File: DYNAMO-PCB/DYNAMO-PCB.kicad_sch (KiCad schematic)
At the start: 12 parts, among them J13 Conn_01x02_Pin, J18 USB3_A, J21 USB3_A, J22 USB3_A, J23 USB3_A, J24 USB3_A, J25 USB3_A, J29 USB_C_Receptacle_USB2.0_16P, J3 Conn_01x03_Pin

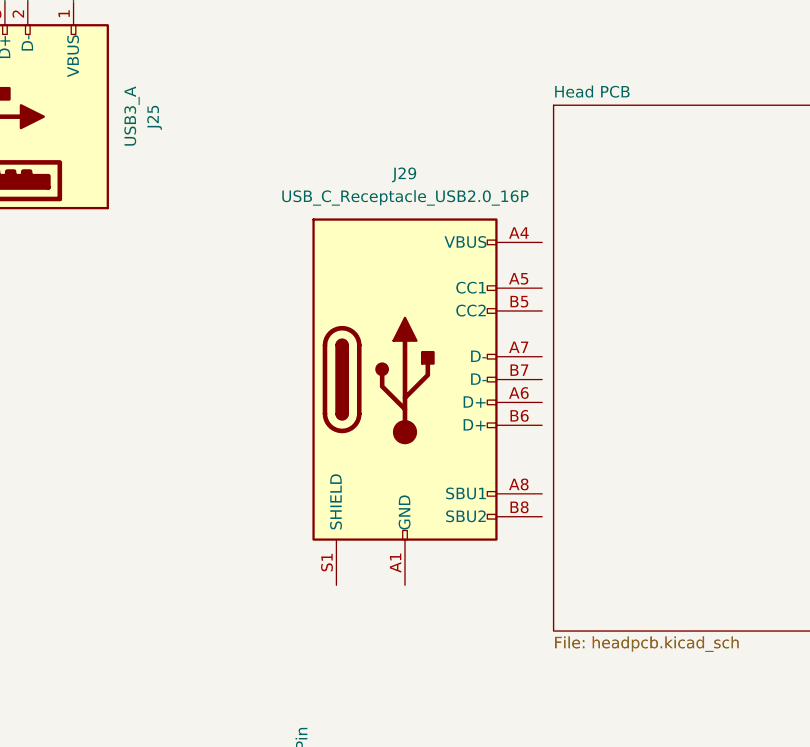
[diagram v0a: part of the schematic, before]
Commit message: wired headpcb sch
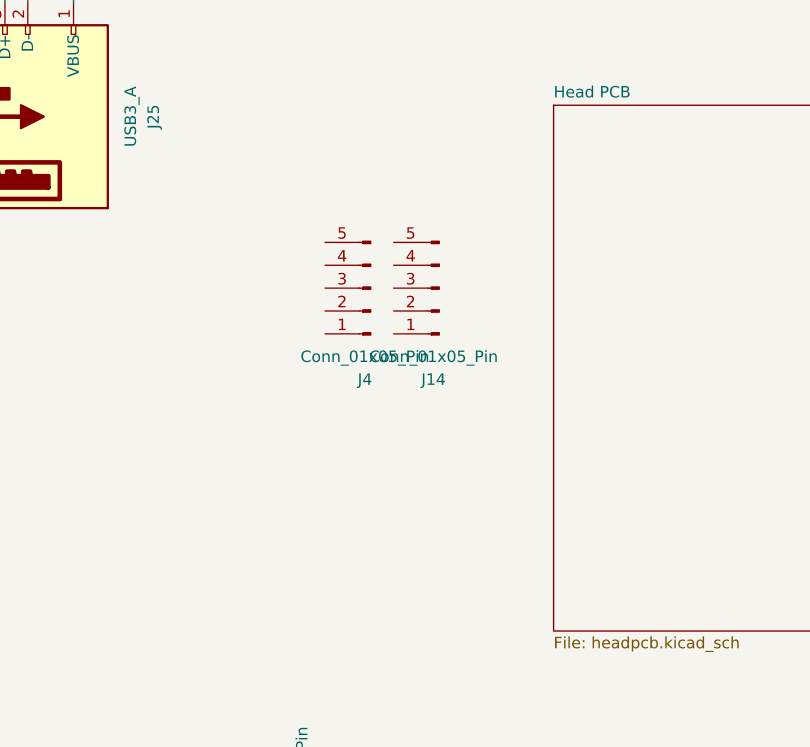
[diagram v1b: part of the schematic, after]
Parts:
- removed J29: USB_C_Receptacle_USB2.0_16P, Connector_USB:USB_C_Receptacle_GCT_USB4105-xx-A_16P_TopMnt_Horizontal, symbol Connector:USB_C_Receptacle_USB2.0_16P
- added J14, J4: Conn_01x05_Pin, Connector_PinHeader_2.54mm:PinHeader_1x05_P2.54mm_Vertical, symbol Connector:Conn_01x05_Pin
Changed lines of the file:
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@@
+	)
+	(symbol
+		(lib_id "Connector:Conn_01x05_Pin")
+		(at 218.44 81.28 180)
+		(unit 1)
+		(exclude_from_sim no)
+		(in_bom yes)
+		(on_board yes)
+		(dnp no)
+		(fields_autoplaced yes)
+		(property "Reference" "J4"
+			(at 217.805 91.44 0)
+			(effects
+				(font
+					(size 1.27 1.27)
+				)
+			)
+		)
+		(property "Value" "Conn_01x05_Pin"
+			(at 217.805 88.9 0)
+			(effects
+				(font
+					(size 1.27 1.27)
+				)
+			)
+		)
+		(property "Footprint" "Connector_PinHeader_2.54mm:PinHeader_1x05_P2.54mm_Vertical"
+			(at 218.44 81.28 0)
+			(effects
+				(font
+					(size 1.27 1.27)
+				)
+				(hide yes)
+			)
+		)
+		(property "Datasheet" "~"
+			(at 218.44 81.28 0)
+			(effects
+				(font
+					(size 1.27 1.27)
+				)
+				(hide yes)
+			)
+		)
+		(property "Description" "Generic connector, single row, 01x05, script generated"
+			(at 218.44 81.28 0)
+			(effects
+				(font
+					(size 1.27 1.27)
+				)
+				(hide yes)
+			)
+		)
+		(pin "1"
+		)
+		(pin "2"
+		)
+		(pin "5"
+		)
+		(pin "3"
+		)
+		(pin "4"
+		)
+		(instances
+			(project ""
+				(path "/2ca9dd43-411d-4cc5-8a4b-ed00d72bae91"
+					(reference "J4")
+					(unit 1)
+				)
+			)
+		)
 	)
 	(symbol
@@
 	)
 	(symbol
-		(lib_id "Connector:USB_C_Receptacle_USB2.0_16P")
-		(at 222.25 91.44 0)
-		(unit 1)
-		(exclude_from_sim no)
-		(in_bom yes)
-		(on_board yes)
-		(dnp no)
-		(fields_autoplaced yes)
-		(property "Reference" "J29"
-			(at 222.25 68.58 0)
-			(effects
-				(font
-					(size 1.27 1.27)
-				)
-			)
-		)
-		(property "Value" "USB_C_Receptacle_USB2.0_16P"
-			(at 222.25 71.12 0)
-			(effects
-				(font
-					(size 1.27 1.27)
-				)
-			)
-		)
-		(property "Footprint" "Connector_USB:USB_C_Receptacle_GCT_USB4105-xx-A_16P_TopMnt_Horizontal"
-			(at 226.06 91.44 0)
-			(effects
-				(font
-					(size 1.27 1.27)
-				)
-				(hide yes)
-			)
-		)
-		(property "Datasheet" "https://www.usb.org/sites/default/files/documents/usb_type-c.zip"
-			(at 226.06 91.44 0)
-			(effects
-				(font
-					(size 1.27 1.27)
-				)
-				(hide yes)
-			)
-		)
-		(property "Description" "USB 2.0-only 16P Type-C Receptacle connector"
-			(at 222.25 91.44 0)
-			(effects
-				(font
-					(size 1.27 1.27)
-				)
-				(hide yes)
-			)
-		)
-		(pin "A1"
-		)
-		(pin "B12"
-		)
-		(pin "B9"
-		)
-		(pin "A4"
-		)
-		(pin "S1"
-		)
-		(pin "A12"
-		)
-		(pin "B1"
-		)
-		(pin "A9"
-		)
-		(pin "B4"
-		)
-		(pin "A7"
-		)
-		(pin "A5"
-		)
-		(pin "B6"
-		)
-		(pin "B5"
-		)
-		(pin "B8"
-		)
-		(pin "B7"
-		)
-		(pin "A6"
-		)
-		(pin "A8"
-		)
-		(instances
-			(project "DYNAMO-PCB"
-				(path "/2ca9dd43-411d-4cc5-8a4b-ed00d72bae91"
-					(reference "J29")
-					(unit 1)
-				)
-			)
-		)
-	)
-	(symbol
 		(lib_id "Connector:USB3_A")
 		(at 101.6 62.23 270)
@@
 					(unit 1)
 				)
+			)
+		)
+	)
+	(symbol
+		(lib_id "Connector:Conn_01x05_Pin")
+		(at 226.06 81.28 180)
+		(unit 1)
+		(exclude_from_sim no)
+		(in_bom yes)
+		(on_board yes)
+		(dnp no)
+		(fields_autoplaced yes)
+		(property "Reference" "J14"
+			(at 225.425 91.44 0)
+			(effects
+				(font
+					(size 1.27 1.27)
+				)
+			)
+		)
+		(property "Value" "Conn_01x05_Pin"
+			(at 225.425 88.9 0)
+			(effects
+				(font
+					(size 1.27 1.27)
+				)
+			)
+		)
+		(property "Footprint" "Connector_PinHeader_2.54mm:PinHeader_1x05_P2.54mm_Vertical"
+			(at 226.06 81.28 0)
+			(effects
+				(font
+					(size 1.27 1.27)
+				)
+				(hide yes)
+			)
+		)
+		(property "Datasheet" "~"
+			(at 226.06 81.28 0)
+			(effects
+				(font
+					(size 1.27 1.27)
+				)
+				(hide yes)
+			)
+		)
+		(property "Description" "Generic connector, single row, 01x05, script generated"
+			(at 226.06 81.28 0)
+			(effects
+				(font
+					(size 1.27 1.27)
+				)
+				(hide yes)
+			)
+		)
+		(pin "1"
+		)
+		(pin "2"
+		)
+		(pin "5"
+		)
+		(pin "3"
+		)
+		(pin "4"
+		)
+		(instances
+			(project "DYNAMO-PCB"
+				(path "/2ca9dd43-411d-4cc5-8a4b-ed00d72bae91"
+					(reference "J14")
+					(unit 1)
+				)

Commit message: schematic wip
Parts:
- removed J14, J4: Conn_01x05_Pin, Connector_PinHeader_2.54mm:PinHeader_1x05_P2.54mm_Vertical, symbol Connector:Conn_01x05_Pin
- added J34: Conn_02x05_Counter_Clockwise, Connector_PinHeader_2.54mm:PinHeader_2x05_P2.54mm_Vertical, symbol Connector_Generic:Conn_02x05_Counter_Clockwise
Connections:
- net GND: now reaches J22.4 (GND), J24.4 (GND)
- net GND: now also C1.2, J13.2 (Pin_2), J18.4 (GND), J21.4 (GND), J23.4 (GND), J25.4 (GND), J3.3 (Pin_3), J34.9 (Pin_9)
- net at J3.1 (Pin_1): now also R1.2
- net Power Distribution/+5V peripherals: now reaches J3.2 (Pin_2)
- net Power Distribution/+5V peripherals: now also C1.1, J13.1 (Pin_1), J34.10 (Pin_10)
- net at A1.11 (D6): now also R1.1
- net at A1.12 (D13): now also J34.8 (Pin_8)
- net at A1.16 (D11): now also J34.7 (Pin_7)
- net at A1.17 (D3/SCL): now also J34.4 (Pin_4)
- net at A1.18 (D10): now also J34.6 (Pin_6)
- net at A1.19 (D2/SDA): now also J34.5 (Pin_5)
- net at A1.20 (D9): now also J34.3 (Pin_3)
- net at A1.22 (D8): now also J34.1 (Pin_1)
- net at A1.24 (D7): now also J34.2 (Pin_2)
- no-connect marks 0 -> 79
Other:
- sheet Power Distribution ports: added +5V peripherals, GND peripherals; removed none
- moved on the sheet: A1A, A1B, C1, J13, J3, R1

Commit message: schematic wip
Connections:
- net Power Distribution/+5V peripherals: now also J3.1 (Pin_1); no longer J3.2 (Pin_2)
- net at R1.2: now also J3.2 (Pin_2); no longer J3.1 (Pin_1)
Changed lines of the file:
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@@
 	(paper "A4")
 	(junction
-		(at 132.08 156.21)
+		(at 128.27 157.48)
 		(diameter 0)
 		(color 0 0 0 0)
@@
 	)
 	(junction
-		(at 132.08 162.56)
-		(diameter 0)
-		(color 0 0 0 0)
-	)
-	(junction
 		(at 173.99 162.56)
 		(diameter 0)
@@
 	)
 	(junction
+		(at 128.27 160.02)
+		(diameter 0)
+		(color 0 0 0 0)
+	)
+	(junction
 		(at 151.13 167.64)
 		(diameter 0)
@@
 	(wire
 		(pts
-			(xy 128.27 160.02) (xy 133.35 160.02)
-		)
-		(stroke
-			(width 0)
-			(type default)
-		)
-	)
-	(wire
-		(pts
 			(xy 229.87 91.44) (xy 228.6 90.17)
 		)
@@
 	(wire
 		(pts
+			(xy 147.32 162.56) (xy 137.16 162.56)
+		)
+		(stroke
+			(width 0)
+			(type default)
+		)
+	)
+	(wire
+		(pts
 			(xy 83.82 67.31) (xy 80.01 63.5)
 		)
@@
 	(wire
 		(pts
-			(xy 132.08 156.21) (xy 133.35 154.94)
+			(xy 130.81 157.48) (xy 133.35 154.94)
 		)
 		(stroke
@@
 	(wire
 		(pts
-			(xy 133.35 160.02) (xy 137.16 156.21)
-		)
-		(stroke
-			(width 0)
-			(type default)
-		)
-	)
-	(wire
-		(pts
 			(xy 157.48 67.31) (xy 154.94 64.77)
 		)
@@
 	(wire
 		(pts
-			(xy 132.08 162.56) (xy 147.32 162.56)
-		)
-		(stroke
-			(width 0)
-			(type default)
-		)
-	)
-	(wire
-		(pts
 			(xy 129.54 44.45) (xy 129.54 49.53)
 		)
@@
 	(wire
 		(pts
+			(xy 137.16 162.56) (xy 134.62 160.02)
+		)
+		(stroke
+			(width 0)
+			(type default)
+		)
+	)
+	(wire
+		(pts
 			(xy 132.08 110.49) (xy 130.81 109.22)
 		)
@@
 	(wire
 		(pts
-			(xy 129.54 166.37) (xy 119.38 166.37)
+			(xy 137.16 132.08) (xy 137.16 160.02)
+		)
+		(stroke
+			(width 0)
+			(type default)
+		)
+	)
+	(wire
+		(pts
+			(xy 129.54 166.37) (xy 121.92 166.37)
 		)
 		(stroke
@@
 	(wire
 		(pts
-			(xy 132.08 156.21) (xy 132.08 162.56)
-		)
-		(stroke
-			(width 0)
-			(type default)
-		)
-	)
-	(wire
-		(pts
 			(xy 213.36 92.71) (xy 215.9 92.71)
 		)
@@
 	(wire
 		(pts
+			(xy 128.27 162.56) (xy 134.62 162.56)
+		)
+		(stroke
+			(width 0)
+			(type default)
+		)
+	)
+	(wire
+		(pts
 			(xy 200.66 80.01) (xy 213.36 92.71)
 		)
@@
 	(wire
 		(pts
-			(xy 130.81 157.48) (xy 132.08 156.21)
-		)
-		(stroke
-			(width 0)
-			(type default)
-		)
-	)
-	(wire
-		(pts
 			(xy 80.01 63.5) (xy 80.01 30.48)
 		)
@@
 	(wire
 		(pts
+			(xy 128.27 157.48) (xy 120.65 157.48)
+		)
+		(stroke
+			(width 0)
+			(type default)
+		)
+	)
+	(wire
+		(pts
 			(xy 229.87 83.82) (xy 228.6 85.09)
 		)
@@
 	(wire
 		(pts
-			(xy 137.16 132.08) (xy 137.16 156.21)
-		)
-		(stroke
-			(width 0)
-			(type default)
-		)
-	)
-	(wire
-		(pts
-			(xy 128.27 162.56) (xy 132.08 162.56)
-		)
-		(stroke
-			(width 0)
-			(type default)
-		)
-	)
-	(wire
-		(pts
 			(xy 180.34 118.11) (xy 213.36 85.09)
 		)
@@
 	(wire
 		(pts
-			(xy 130.81 157.48) (xy 118.11 157.48)
+			(xy 130.81 157.48) (xy 128.27 157.48)
 		)
 		(stroke
@@
 	(wire
 		(pts
+			(xy 128.27 160.02) (xy 134.62 160.02)
+		)
+		(stroke
+			(width 0)
+			(type default)
+		)
+	)
+	(wire
+		(pts
 			(xy 118.11 46.99) (xy 121.92 46.99)
 		)
@@
 	(wire
 		(pts
-			(xy 119.38 166.37) (xy 115.57 162.56)
+			(xy 121.92 166.37) (xy 118.11 162.56)
 		)
 		(stroke
@@
 	(wire
 		(pts
-			(xy 118.11 157.48) (xy 115.57 160.02)
+			(xy 120.65 157.48) (xy 118.11 160.02)
 		)
 		(stroke
@@
 	(wire
 		(pts
+			(xy 128.27 157.48) (xy 128.27 160.02)
+		)
+		(stroke
+			(width 0)
+			(type default)
+		)
+	)
+	(wire
+		(pts
 			(xy 81.28 31.75) (xy 83.82 29.21)
+		)
+		(stroke
+			(width 0)
+			(type default)
+		)
+	)
+	(wire
+		(pts
+			(xy 137.16 160.02) (xy 134.62 162.56)
 		)
 		(stroke
@@
 					(size 1.27 1.27)
 				)
+				(hide yes)
 			)
 		)
@@
 					(size 1.27 1.27)
 				)
+				(hide yes)
 			)
 		)
@@
 	(symbol
 		(lib_id "Connector:Conn_01x02_Pin")
-		(at 110.49 160.02 0)
+		(at 113.03 160.02 0)
 		(unit 1)
 		(exclude_from_sim no)
@@
 		(dnp no)
 		(property "Reference" "J13"
+			(at 114.9351 163.83 90)
+			(effects
+				(font
+					(size 1.27 1.27)
+				)
+				(justify right)
+				(hide yes)
+			)
+		)
+		(property "Value" "Conn_01x02_Pin"
 			(at 112.3951 163.83 90)
 			(effects
@@
 				)
 				(justify right)
-			)
-		)
-		(property "Value" "Conn_01x02_Pin"
-			(at 109.8551 163.83 90)
-			(effects
-				(font
-					(size 1.27 1.27)
-				)
-				(justify right)
+				(hide yes)
 			)
 		)
 		(property "Footprint" "Connector_PinHeader_2.54mm:PinHeader_1x02_P2.54mm_Vertical"
-			(at 110.49 160.02 0)
+			(at 113.03 160.02 0)
 			(effects
 				(font
@@
 		)
 		(property "Datasheet" "~"
-			(at 110.49 160.02 0)
+			(at 113.03 160.02 0)
 			(effects
 				(font
@@
 		)
 		(property "Description" "Generic connector, single row, 01x02, script generated"
-			(at 110.49 160.02 0)
-			(effects
-				(font
+			(at 113.03 160.02 0)
+			(effects
+				(font

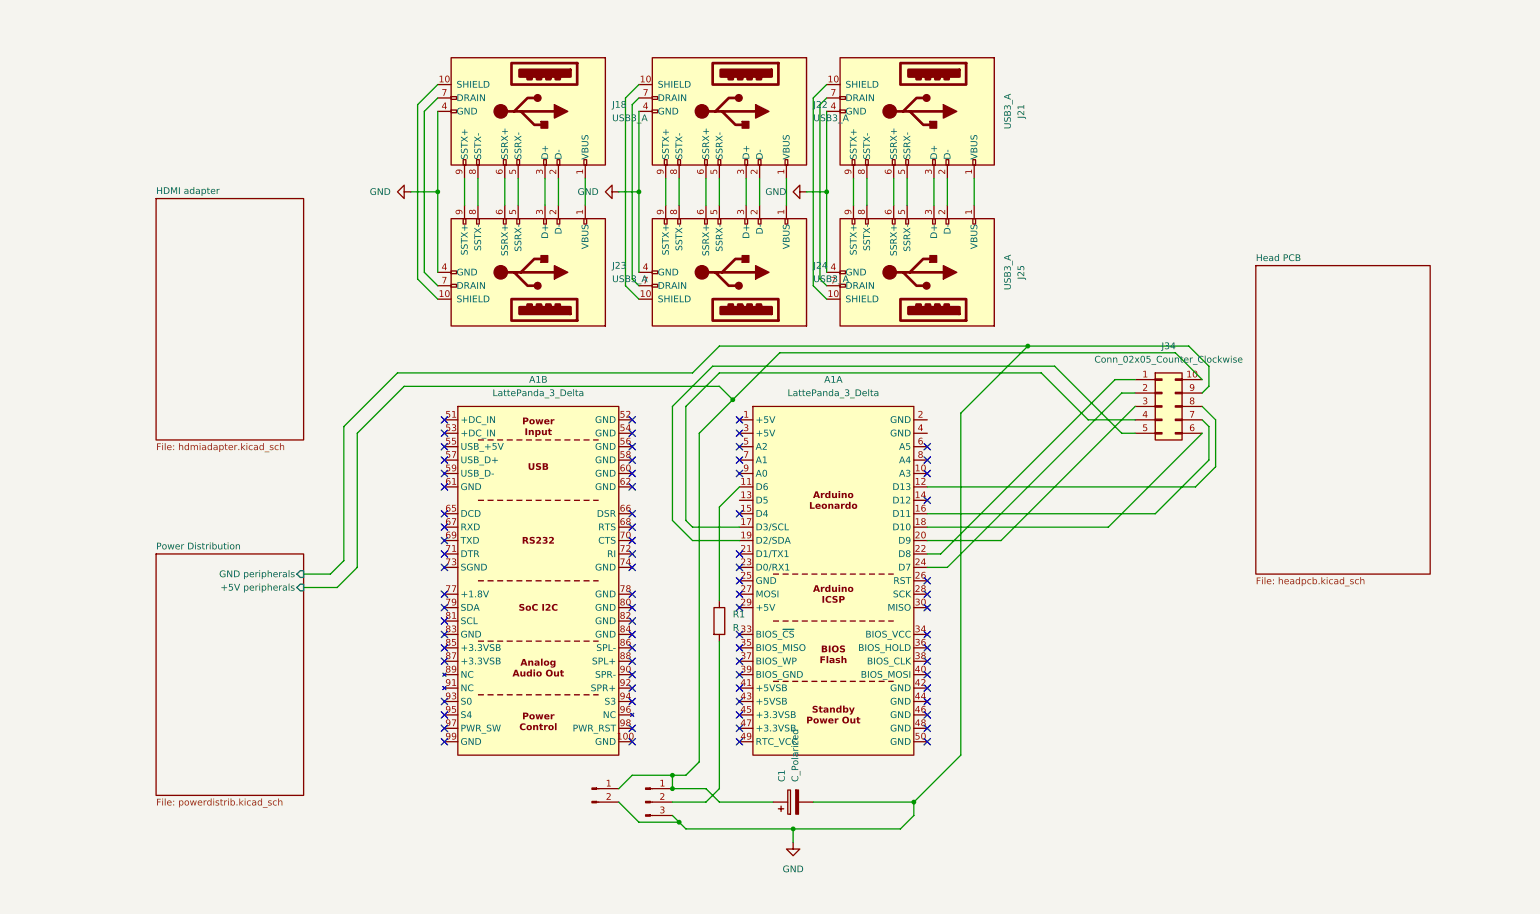
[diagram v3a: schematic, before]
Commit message: schematic complete (pre-ERC)
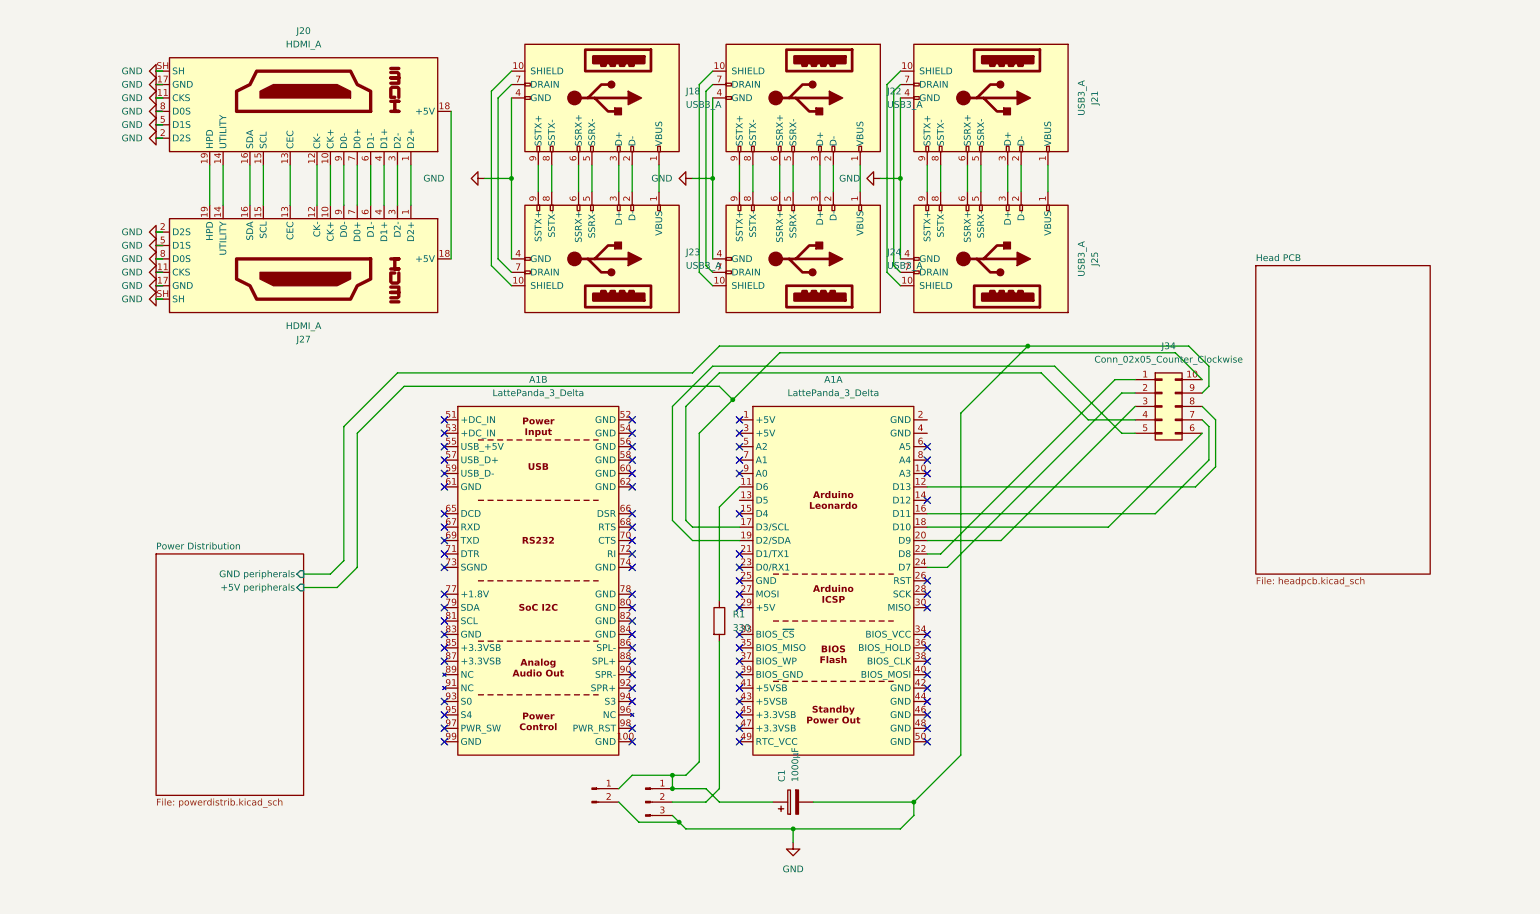
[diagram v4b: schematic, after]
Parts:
- added J20, J27: HDMI_A, Connector_Video:HDMI_A_Molex_208658-1001_Horizontal, symbol Connector:HDMI_A
- C1: value C_Polarized -> 1000µF
- R1: value R -> 330
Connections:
- net GND: now also J20.11 (CKS), J20.17 (GND), J20.2 (D2S), J20.5 (D1S), J20.8 (D0S), J20.SH, J27.11 (CKS), J27.17 (GND), J27.2 (D2S), J27.5 (D1S), J27.8 (D0S), J27.SH
- new net: J20.1 (D2+), J27.1 (D2+)
- new net: J20.10 (CK+), J27.10 (CK+)
- new net: J20.12 (CK-), J27.12 (CK-)
- new net: J20.13 (CEC), J27.13 (CEC)
- new net: J20.14 (UTILITY), J27.14 (UTILITY)
- new net: J20.15 (SCL), J27.15 (SCL)
- new net: J20.16 (SDA), J27.16 (SDA)
- new net: J20.18 (+5V), J27.18 (+5V)
- new net: J20.19 (HPD), J27.19 (HPD)
- new net: J20.3 (D2-), J27.3 (D2-)
- new net: J20.4 (D1+), J27.4 (D1+)
- new net: J20.6 (D1-), J27.6 (D1-)
- new net: J20.7 (D0+), J27.7 (D0+)
- new net: J20.9 (D0-), J27.9 (D0-)
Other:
- removed sheet HDMI adapter
- moved on the sheet: J18, J21, J22, J23, J24, J25
